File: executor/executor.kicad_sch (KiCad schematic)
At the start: 132 parts, among them J1 XT30PW(2+2), J2 gh1.25, 3p, J3 Conn_01x04, Q1 WNM6006, Q2 WNM6006, Q3 WNM6006, Q4 WNM6006, Q5 WNM6006, Q6 WNM6006, U1 WD1601E, U2 DRV8323SRTAT, U3 GD32F303RETx, U4 TCAN4550RGYRQ1, U5 AS5047P-ATSM, U6 QMA7981, Y1 8M, Y2 40M

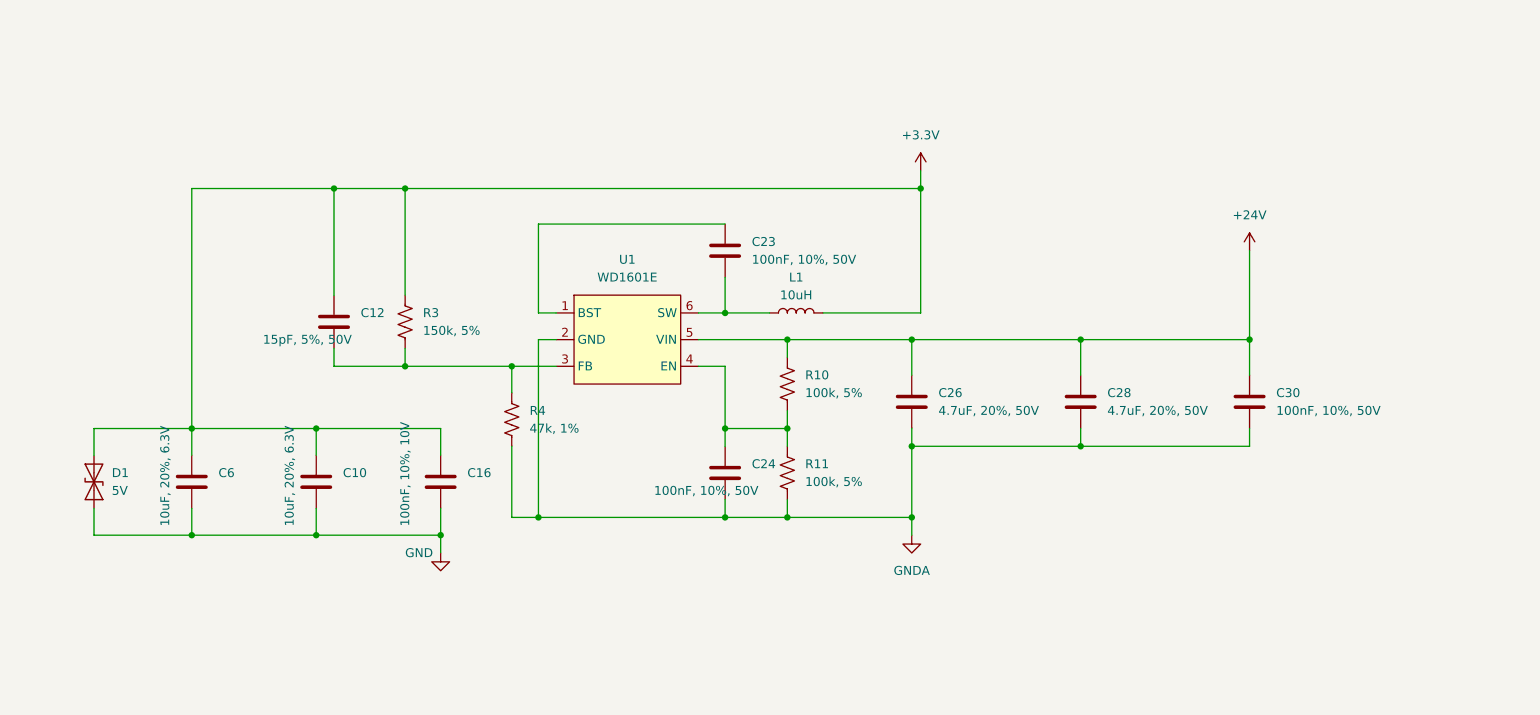
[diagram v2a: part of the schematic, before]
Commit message: [Fix] Replace dc-dc module to tps & fix xt30-2+2 position
Signed-off-by: Homalozoa <nx.tardis@gmail.com>
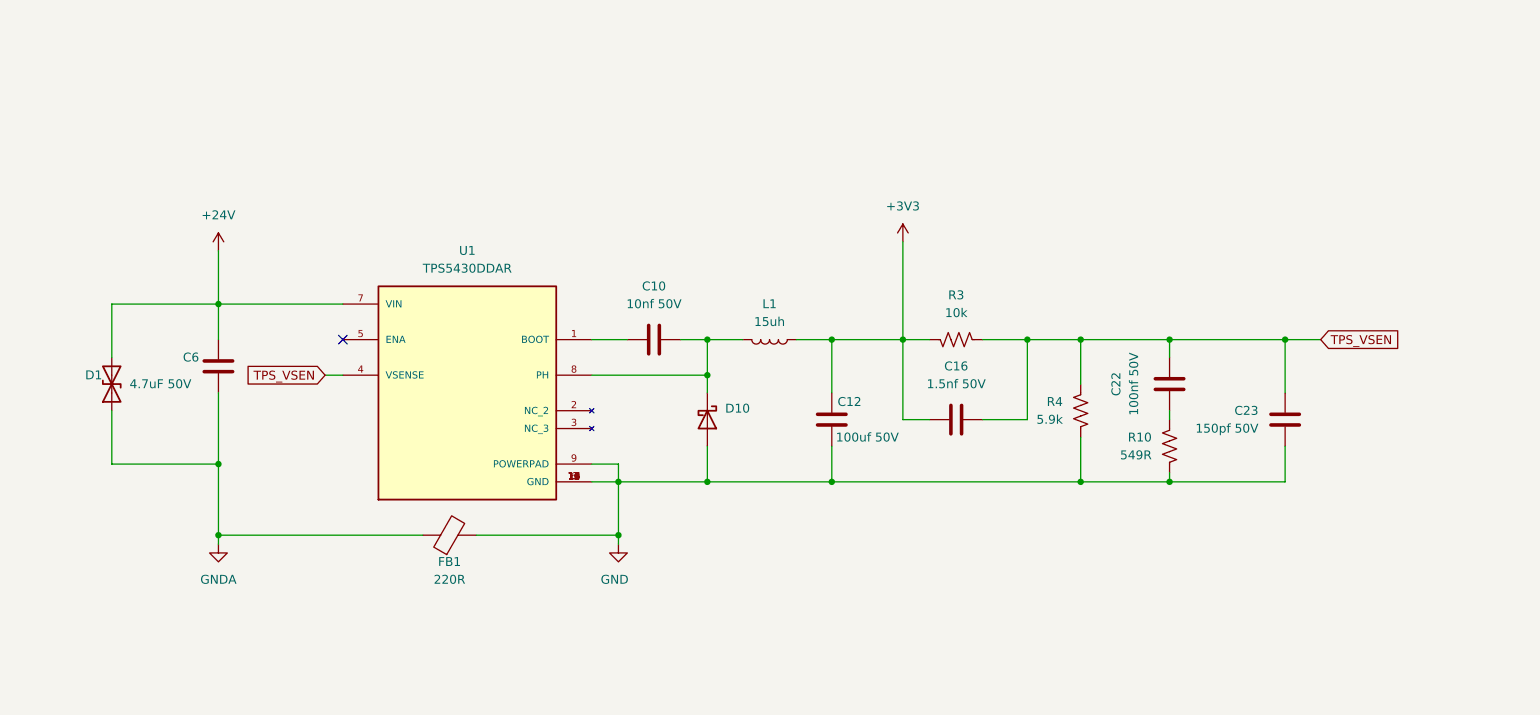
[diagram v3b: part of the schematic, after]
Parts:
- removed C24, C30: 100nF, 10%, 50V, Capacitor_SMD:C_0402_1005Metric, symbol Device:C
- removed C26, C28: 4.7uF, 20%, 50V, Capacitor_SMD:C_0805_2012Metric, symbol Device:C
- removed D1: 5V, Diode_SMD:D_SOD-923, symbol Diode:ESD9B5.0ST5G
- removed R11: 100k, 5%, Resistor_SMD:R_0402_1005Metric, symbol Device:R_US
- removed U1: WD1601E, Package_TO_SOT_SMD:SOT-23-6, symbol Rolling_Custom:WD1601E
- added C22: 100nf 50V, Capacitor_SMD:C_0402_1005Metric, symbol Device:C
- added D1: (no value), symbol Device:D_TVS
- added D10: (no value), symbol Diode:B340
- added FB1: 220R, Resistor_SMD:R_0603_1608Metric, symbol Device:FerriteBead
- added U1: TPS5430DDAR, Rolling_Custom:TPS5430DDAR, symbol Rolling_Custom:TPS5430DDAR
- C10: value 10uF, 20%, 6.3V -> 10nf 50V
- C12: value 15pF, 5%, 50V -> 100uf 50V; footprint Capacitor_SMD:C_0402_1005Metric -> Capacitor_SMD:C_0805_2012Metric
- C16: value 100nF, 10%, 10V -> 1.5nf 50V
- C23: value 100nF, 10%, 50V -> 150pf 50V
- C6: value 10uF, 20%, 6.3V -> 4.7uF 50V; footprint Capacitor_SMD:C_0402_1005Metric -> Capacitor_SMD:C_0805_2012Metric
- L1: value 10uH -> 15uh
- R10: value 100k, 5% -> 549R; footprint Resistor_SMD:R_0402_1005Metric -> Resistor_SMD:R_0201_0603Metric
- R3: value 150k, 5% -> 10k
- R4: value 47k, 1% -> 5.9k
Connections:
- net +24V: now also C6.1, D1.2 (A2), U1.7 (VIN); no longer R10.1
- net +3V3: now also C12.2, C16.2, L1.1, R3.2; no longer C10.1, C12.1, C16.1, C6.1, L1.2, R3.1
- net GND: now also C12.1, C23.2, R10.2, R4.2, D10.2 (A), FB1.2, U1.10 (GND), U1.11 (GND), U1.12 (GND), U1.13 (GND), U1.14 (GND), U1.15 (GND), U1.16 (GND), U1.17 (GND), U1.6 (GND), U1.9 (POWERPAD); no longer C10.2, C16.2, C6.2
- net GNDA: now also C6.2, D1.1 (A1), FB1.1; no longer R4.2
- net TPS_VSEN: now reaches C23.1
- net TPS_VSEN: now also C16.1, R3.1, R4.1, C22.1, U1.4 (VSENSE)
- new net: C22.2, R10.1
- new net: C10.2, D10.1 (K), L1.2, U1.8 (PH)
- new net: C10.1, U1.1 (BOOT)
- no-connect marks 30 -> 31

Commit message: [New] Replace TI's solution with TMC's in executor prj
1. DRV8323 --> TMC6200
2. GD32F303 --> TMC4671 + GD32C103
3. TCAN4550 --> GD32C103
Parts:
- removed C16: 1.5nf 50V, Capacitor_SMD:C_0402_1005Metric, symbol Device:C
- removed C22: 100nf 50V, Capacitor_SMD:C_0402_1005Metric, symbol Device:C
- removed C23: 150pf 50V, Capacitor_SMD:C_0402_1005Metric, symbol Device:C
- removed C25, C37: 1uF, 10%, 50V, Capacitor_SMD:C_0603_1608Metric, symbol Device:C
- removed C31, C34: 4.7uF, 20%, 50V, Capacitor_SMD:C_0805_2012Metric, symbol Device:C
- removed C32, C35: 1nF, 10%, 50V, Capacitor_SMD:C_0402_1005Metric, symbol Device:C
- removed C36: 100nF, 10%, 50V, Capacitor_SMD:C_0402_1005Metric, symbol Device:C
- removed C38: 20pF, 10%, 10V, Capacitor_SMD:C_0402_1005Metric, symbol Device:C
- removed C39: 100nF, 10%, 10V, Capacitor_SMD:C_0402_1005Metric, symbol Device:C
- removed C40: 10uF, 10%, 10V, Capacitor_SMD:C_0402_1005Metric, symbol Device:C
- removed C59: 470nF, 10%, 50V, Capacitor_SMD:C_0603_1608Metric, symbol Device:C
- removed D10: (no value), symbol Diode:B340
- removed D2, D4, D5, D6: BAV99, Package_TO_SOT_SMD:SOT-23, symbol Diode:BAV99
- removed D3: 30V, Diode_SMD:D_SMA, symbol Device:D_TVS
- removed D7: Blue, LED_SMD:LED_0402_1005Metric, symbol Device:LED
- removed D8, D9: 12V, Diode_SMD:D_SOD-323, symbol Device:D_TVS
- removed FB1: 220R, Resistor_SMD:R_0603_1608Metric, symbol Device:FerriteBead
- removed J1: XT30PW(2+2), Rolling_Custom:XT30PW(2+2), symbol Rolling_Custom:XT30PW(2+2)
- removed J2: gh1.25, 3p, Connector_JST:JST_GH_SM03B-GHS-TB_1x03-1MP_P1.25mm_Horizontal, symbol Connector:Conn_01x03_Female
- removed L1: 15uh, Inductor_SMD:L_0603_1608Metric, symbol Device:L
- removed NT1: NetTie, NetTie:NetTie-2_SMD_Pad0.5mm, symbol Device:NetTie_2
- removed Q1, Q2, Q3, Q4, Q5, Q6: WNM6006, Rolling_Custom:PDFN5X6-8L, symbol Rolling_Custom:WNM6006
- removed R27: 10k, 5%, Resistor_SMD:R_0402_1005Metric, symbol Device:R_US
- removed R30: 0R, 5%, Resistor_SMD:R_0402_1005Metric, symbol Device:R_US
- removed R4: 5.9k, Resistor_SMD:R_0402_1005Metric, symbol Device:R_US
- removed TP10: C, TestPoint:TestPoint_Plated_Hole_D2.0mm, symbol Connector:TestPoint
- removed TP7: A, TestPoint:TestPoint_Plated_Hole_D2.0mm, symbol Connector:TestPoint
- removed TP8: B, TestPoint:TestPoint_Plated_Hole_D2.0mm, symbol Connector:TestPoint
- removed U1: TPS5430DDAR, Rolling_Custom:TPS5430DDAR, symbol Rolling_Custom:TPS5430DDAR
- removed U2: DRV8323SRTAT, Rolling_Custom:WQFN40, symbol Rolling_Custom:DRV8323SRTAT
- removed U3: GD32F303RETx, Package_QFP:LQFP-64_10x10mm_P0.5mm, symbol Rolling_Custom:GD32F303RETx
- removed U4: TCAN4550RGYRQ1, Rolling_Custom:VQFN20, symbol Rolling_Custom:TCAN4550RGYRQ1
- removed Y2: 40M, Oscillator:Oscillator_SMD_ECS_2520MV-xxx-xx-4Pin_2.5x2.0mm, symbol Device:Crystal_GND24
- added C1, C11, C13, C3, C4, C63, C7, C8: 100nF/50V/0402, Capacitor_SMD:C_0402_1005Metric, symbol Device:C
- added C14: 22nF/50V/0603, Capacitor_SMD:C_0603_1608Metric, symbol Device:C
- added C19, C26: 100nF/100V/0805, Capacitor_SMD:C_0805_2012Metric, symbol Device:C
- added C2: 4.7uF/50V/0402, Capacitor_SMD:C_0402_1005Metric, symbol Device:C
- added C28, C30: 470nF/50V/0603, Capacitor_SMD:C_0603_1608Metric, symbol Device:C
- added C56: 4.7uF/10V/0402, Capacitor_SMD:C_0402_1005Metric, symbol Device:C
- added C57: 20pF/10V/0402, Capacitor_SMD:C_0402_1005Metric, symbol Device:C
- added C58: 1uF/10V/0402, Capacitor_SMD:C_0402_1005Metric, symbol Device:C
- added C61: 8.2nf/50V/0603, Capacitor_SMD:C_0603_1608Metric, symbol Device:C
- added C67: 22uF/6.3V/0402, Capacitor_SMD:C_0402_1005Metric, symbol Device:C
- added C68, C69: 47uf/50V/0603, Capacitor_SMD:C_0603_1608Metric, symbol Device:C
- added C71, C72: 100pF/50V/0402, Capacitor_SMD:C_0402_1005Metric, symbol Device:C
- added C73: 2.2uF/50V/0603, Capacitor_SMD:C_0603_1608Metric, symbol Device:C
- added C9: 2.2uF/100V/1210, Capacitor_SMD:C_1210_3225Metric, symbol Device:C
- added D2: BZT52C24, Diode_SMD:D_SOD-123F, symbol Diode:BZT52Bxx
- added D3: BZT52C5V1S, Diode_SMD:D_SOD-123F, symbol Diode:BZT52Bxx
- added D4, D5: 12V, Diode_SMD:D_SOD-323, symbol Device:D_TVS
- added J1: PowerOutput, Connector_AMASS:AMASS_XT30UPB-M_1x02_P5.0mm_Vertical, symbol Connector:Conn_01x02_Female
- added J2: SWD_DBG_Mounting, Connector_JST:JST_GH_SM03B-GHS-TB_1x03-1MP_P1.25mm_Horizontal, symbol Connector_Generic_MountingPin:Conn_01x03_MountingPin
- added J4: CAN_FD, Connector_JST:JST_GH_SM04B-GHS-TB_1x04-1MP_P1.25mm_Horizontal, symbol Connector_Generic_MountingPin:Conn_01x04_MountingPin
- added J5: RTMI, Rolling_Custom:FH34SRJ-6S-0.5SH50, symbol Connector_Generic:Conn_01x08
- added L3: 15uh, SLO0530H150MTT, Inductor_SMD:L_Sunlord_MWSA0518_5.4x5.2mm, symbol Device:L
- added L4: LQW15AN1N3D10D, Inductor_SMD:L_0402_1005Metric, symbol Device:L
- added Q1, Q2, Q3, Q4, Q5, Q6: BSC0702LS, Package_TO_SOT_SMD:TDSON-8-1, symbol Transistor_FET:BSC070N10NS5
- added R11: 22R/1%/0603, Resistor_SMD:R_0603_1608Metric, symbol Device:R_US
- added R17: 1k/1%/0603, Resistor_SMD:R_0603_1608Metric, symbol Device:R_US
- added R2: 0.003R/1%/1W/1206, Resistor_SMD:R_1206_3216Metric, symbol Device:R_US
- added R24: 20.5k/0402, Resistor_SMD:R_0402_1005Metric, symbol Device:R_US
- added R25: 10k/5%/0402, Resistor_SMD:R_0402_1005Metric, symbol Device:R_US
- added R35, R36: 0R/0402, Resistor_SMD:R_0402_1005Metric, symbol Device:R_US
- added TP1: U, TestPoint:TestPoint_Plated_Hole_D2.0mm, symbol Connector:TestPoint
- added TP2: V, TestPoint:TestPoint_Plated_Hole_D2.0mm, symbol Connector:TestPoint
- added TP3: W, TestPoint:TestPoint_Plated_Hole_D2.0mm, symbol Connector:TestPoint
- added U1: TMC4671-LA, Rolling_Custom:QFN76_10P5X6P5_TRI, symbol Rolling_Custom:TMC4671-LA
- added U2: TJA1042T, Package_SO:SOIC-8_3.9x4.9mm_P1.27mm, symbol Interface_CAN_LIN:TJA1042T
- added U3: TMC6200-TA, Rolling_Custom:eTQFP48_9x9_TRI, symbol Rolling_Custom:TMC6200-TA
- added U6: TPS54231, Package_SO:SOIC-8_3.9x4.9mm_P1.27mm, symbol Regulator_Switching:TPS54233
- added U7: AMS1117-3.3, Package_TO_SOT_SMD:SOT-223-3_TabPin2, symbol Regulator_Linear:AMS1117-3.3
- added U8: GD32C103TBUx, Rolling_Custom:QFN-36-1EP_6x6mm_P0.5mm, symbol Rolling_Custom:GD32C103TBUx
- added X1: XO32, Oscillator:Oscillator_SMD_EuroQuartz_XO32-4Pin_3.2x2.5mm, symbol Oscillator:XO32
- C10: value 10nf 50V -> 2.2uF/100V/1210; footprint Capacitor_SMD:C_0402_1005Metric -> Capacitor_SMD:C_1210_3225Metric
- C12: value 100uf 50V -> 2.2uF/50V/0603; footprint Capacitor_SMD:C_0805_2012Metric -> Capacitor_SMD:C_0603_1608Metric
- C15: renamed from C1; value 10uF, 20%, 50V -> 10uF/50V/0805
- C16: renamed from C2; value 10uF, 20%, 50V -> 10uF/50V/0805
- C17: renamed from C61; value 100nF, 10%, 10V -> 100nF/10V/0402
- C18: renamed from C3; value 10uF, 20%, 50V -> 10uF/50V/0805
- C20: renamed from C4; value 10uF, 20%, 50V -> 10uF/50V/0805
- C21: renamed from C63; value 1uF, 10%, 10V -> 1uF/10V/0402
- C22: renamed from C5; value 10uF, 20%, 50V -> 10uF/50V/0805
- C23: renamed from C7; value 10uF, 20%, 50V -> 10uF/50V/0805
- C24: renamed from C8; value 10uF, 20%, 50V -> 10uF/50V/0805
- C25: renamed from C9; value 10uF, 20%, 50V -> 10uF/50V/0805
- C27: renamed from C11; value 10uF, 20%, 50V -> 10uF/50V/0805
- C29: value 1uF, 10%, 50V -> 470nF/50V/0603
- C31: renamed from C13; value 10uF, 20%, 50V -> 10uF/50V/0805
- C32: renamed from C56; value 10nF, 10%, 10V -> 10nF/10V/0402
- C33: renamed from C14; value 10uF, 20%, 50V -> 10uF/50V/0805
- C34: renamed from C15; value 10uF, 20%, 50V -> 10uF/50V/0805
- C35: renamed from C57; value 2.2uF, 10%, 10V -> 2.2uF/10V0402
- C36: renamed from C18; value 10uF, 20%, 50V -> 10uF/50V/0805
- C37: renamed from C19; value 10uF, 20%, 50V -> 10uF/50V/0805
- C38: renamed from C58; value 100nnF, 10%, 10V -> 100nF/10V/0402
- C39: renamed from C20; value 10uF, 20%, 50V -> 10uF/50V/0805
- C40: renamed from C21; value 10uF, 20%, 50V -> 10uF/50V/0805
- C41: value 100nF, 10%, 10V -> 10pf/50V/0402
- C42: value 20pF, 10%, 10V -> 10uF/10V/0402
- C43: value 100nF, 10%, 10V -> 100nF/50V/0402
- C44, C46, C52: value 100nF, 10%, 10V -> 100nF/10V/0402
- C45: value 10uF, 10%, 10V -> 1.5nf/50V/0603; footprint Capacitor_SMD:C_0402_1005Metric -> Capacitor_SMD:C_0603_1608Metric
- C47: value 4.7uF, 10%, 10V -> 10uF/10V/0402
- C48: value 1uF, 10%, 10V -> 100nF/10V/0402
- C49: value 47nF, 10%, 50V -> 100nF/10V/0402
- C5: renamed from C17; value 1uF, 10%, 50V -> 2.2uF/100V/1210; footprint Capacitor_SMD:C_0603_1608Metric -> Capacitor_SMD:C_1210_3225Metric
- C50: value 1uF, 10%, 10V -> 20pF/10V/0402
- C51: value 100nF, 10%, 10V -> 4.7uF/50V/0805; footprint Capacitor_SMD:C_0402_1005Metric -> Capacitor_SMD:C_0805_2012Metric
- C53: value 10pF, 10%, 50V -> 100nF/50V/0402
- C54: value 10nF, 10%, 50V -> 4.7uF/50V/0805; footprint Capacitor_SMD:C_0402_1005Metric -> Capacitor_SMD:C_0805_2012Metric
- C55: value 10pF, 10%, 50V -> 10uf/50V/0402
- C59: renamed from C27; value 100nF, 10%, 10V -> 100nF/10V/0402
- C6: value 4.7uF 50V -> 100nF/50V/0402; footprint Capacitor_SMD:C_0805_2012Metric -> Capacitor_SMD:C_0402_1005Metric
- C60: value 100pF, 10%, 10V -> 100nF/10V/0402
- C62: value 100pF, 10%, 10V -> 10uf/50V/0402
- C64: value 100nF, 10%, 50V -> 100nF/10V/0402
- C65: value 10uF, 10%, 50V -> 10uf/50V/0402; footprint Capacitor_SMD:C_0603_1608Metric -> Capacitor_SMD:C_0402_1005Metric
- C66: value 10uF, 10%, 50V -> 100nF/50V/0402; footprint Capacitor_SMD:C_0603_1608Metric -> Capacitor_SMD:C_0402_1005Metric
- C70: renamed from C33; value 100nF, 10%, 10V -> 100nF/10V/0402
- D1: value (none) -> SMF30CA; footprint (none) -> Diode_SMD:D_SOD-123
- J3: value Conn_01x04 -> SWD_DBG
- L2: value 20R -> FCM1608KF-100T07; footprint Resistor_SMD:R_0402_1005Metric -> Resistor_SMD:R_0603_1608Metric
- R1, R12, R13, R7: value 0 -> 22R/1%/0603; footprint Resistor_SMD:R_0402_1005Metric -> Resistor_SMD:R_0603_1608Metric
- R10: value 549R -> 22R/1%/0603; footprint Resistor_SMD:R_0201_0603Metric -> Resistor_SMD:R_0603_1608Metric
- R14: renamed from R36; value 2.2k, 5% -> 4.7k/5%/0402
- R15: renamed from R37; value 2.2k, 5% -> 4.7k/5%/0402
- R16: value 0.001R -> 4k7/1%/0603; footprint Resistor_SMD:R_1206_3216Metric -> Resistor_SMD:R_0603_1608Metric
- R18: value 10k, 5% -> 64.9k/0402
- R19: value 0 -> 0r/0402
- R20: value 10k, 5% -> 10k/5%/0402
- R21, R22: value 100R, 5% -> 4k7/1%/0603; footprint Resistor_SMD:R_0402_1005Metric -> Resistor_SMD:R_0603_1608Metric
- R23: value 100R, 5% -> 169k/0402
- R26: renamed from R14; value 10k, 5% -> 10k/5%/0402
- R27: renamed from R15; value 10k, 5% -> 10k/5%/3477K/0402
- R28: value 0R, 5% -> 10.2k/0402
- R29: value 0R, 5% -> 1.96k/0402
- R3: value 10k -> 0.003R/1%/1W/1206; footprint Resistor_SMD:R_0402_1005Metric -> Resistor_SMD:R_1206_3216Metric
- R30: renamed from R17; value 10k, 5% -> 10k/5%/0402
- R31: value 100R, 5% -> 120R/0402
- R32: value 33k -> 4.7k/5%/0402
- R33: value 330R, 5% -> 0R/0402
- R34: value 3k -> 0R/0402
- R4: renamed from R2; value 0 -> 22R/1%/0603; footprint Resistor_SMD:R_0402_1005Metric -> Resistor_SMD:R_0603_1608Metric
- R5: value 150k, 5% -> 22R/1%/0603; footprint Resistor_SMD:R_0402_1005Metric -> Resistor_SMD:R_0603_1608Metric
- R6: value 10k, 5% -> 10k/1%/0402
- R8: value 0 -> 0.003R/1%/1W/1206; footprint Resistor_SMD:R_0402_1005Metric -> Resistor_SMD:R_1206_3216Metric
- R9: value 0.001R -> 0.003R/1%/1W/1206
- renumbered TP13 to TP4, TP14 to TP5, U6 to U4
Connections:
- net CAN_H is gone; now on net GND: C62.2
- net CAN_L is gone; now on net GND: C60.2
- net ECD_MISO is gone; now on an unnamed net: U5.3 (MISO)
- net IBP is gone; now on net V: R9.1
- net ISENSE_A is gone; now on net +5V: R21.1
- net ISENSE_B is gone; now on net +2.5V_REF: R22.1
- net ISENSE_C is gone; now on net +24V: R23.1
- net PWM_A is gone; now on net 5V_FB: R28.2
- net PWM_B is gone; now on net GND: R29.2
- net TCAN_OSC_IN is gone; now on net +2.5V_REF: C53.2
- net TCAN_OSC_OUT is gone; now on net GND: C55.2
- net TPS_VSEN is gone; now on net U: R3.1
- net VGL_B is gone; now on net V: R8.1
- net +24V: now also C10.2, C51.1, C54.1, C55.1, R16.1, C11.2, C19.1, C26.1, C9.2, D2.1 (K), J1.2 (Pin_2), Q1.5 (D), Q3.5 (D), Q5.5 (D), U3.29 (VSA), U3.33 (VS), U6.2 (VIN); no longer C29.2, C6.1, C64.1, C65.1, R34.1, R5.1
- net +3V3: now also C42.2, C44.2, C49.1, C60.1, R20.1, R32.2, R6.1, C1.2, C13.2, C56.1, C58.1, L4.2, R36.2, U1.13 (VCCIO2), U1.2 (VCCIO1), U1.43 (VCCIO3), U1.52 (VCCIO4), U1.61 (VCCIO5), U1.72 (VCCIO6), U3.19 (VCC_IO), U8.1 (VDD), U8.19 (VDD), U8.27 (VDD), X1.4 (V+); no longer C12.2, C41.1, C43.2, C44.1, C47.1, C50.1, C51.1, R18.1, R20.2, R3.2, U4.10 (SENB/SCS)
- net ACC_INT1: now also U8.32 (PB5)
- net ACC_INT2: now also U8.31 (PB4)
- net ACC_SCL: now also U8.33 (PB6)
- net ACC_SDA: now also U8.34 (PB7)
- net DRV_EN: now also U1.32 (ENO), U3.27 (DRV_EN)
- net DRV_SCS: now also U3.13 (CSN_IDRV0), U8.20 (PA8)
- net ECD_SCS: now also R34.2, U8.21 (PA9); no longer U5.1 (CSN)
- net GND: now also C10.1, C15.2, C16.2, C18.2, C20.2, C22.2, C23.2, C24.2, C25.2, C27.2, C31.2, C33.2, C34.2, C36.2, C37.2, C39.2, C40.2, C44.1, C45.2, C46.2, C49.2, C5.1, C50.1, C54.2, C6.1, D1.1 (A1), R22.2, C1.1, C11.1, C13.1, C2.2, C26.2, C3.1, C4.1, C56.2, C57.1, C58.2, C61.2, C63.2, C67.2, C68.2, C69.2, C7.1, C71.1, C72.1, C73.1, C8.1, C9.1, D2.2 (A), D3.2 (A), D4.2 (A2), D5.2 (A2), J1.1 (Pin_1), J2.3 (Pin_3), J2.MP (MountPin), J4.MP (MountPin), J5.6 (Pin_6), J5.7 (Pin_7), J5.8 (Pin_8), Q2.1 (S), Q2.2 (S), Q2.3 (S), Q4.1 (S), Q4.2 (S), Q4.3 (S), Q6.1 (S), Q6.2 (S), Q6.3 (S), R17.2, R24.2, R25.2, U1.14 (GNDIO2), U1.24 (GNDA), U1.3 (GNDIO1), U1.44 (GNDIO3), U1.53 (GNDIO4), U1.54 (TEST), U1.59 (PWM_IDLE_H), U1.60 (PWM_IDLE_L), U1.62 (GNDIO5), U1.73 (GNDIO6), U1.77 (EPAD), U2.2 (GND), U3.24 (CLK), U3.8 (GNDA), U3.EPAD, U6.7 (GND), U7.1 (GND), U8.18 (VSS), U8.26 (VSS), U8.36 (VSS), X1.2 (GND); no longer C44.2, C47.2, C48.2, C50.2, C54.1, C55.1, C60.1, C62.1, C64.2, R10.2, R33.2, R6.2
- net MCU_OSC_IN: now also C50.2, U8.2 (PD0-OSCIN)
- net MCU_OSC_OUT: now also C57.2, U8.3 (PD1-OSCOUT); no longer C42.2
- net NRST: now also C46.1, R20.2, U8.4 (NRST); no longer R18.2
- net SWCLK: now also J2.2 (Pin_2), U8.28 (PA14)
- net SWDIO: now also J2.1 (Pin_1), U8.25 (PA13)
- net TEMP_BOARD: now also U8.8 (PA1)
- net TEMP_MOTOR: now also U8.7 (PA0)
- net HSV: now reaches R10.1
- net HSV: now also U3.43 (HSV)
- net CANFD_H: now reaches R31.1
- net CANFD_H: now also C72.2, D5.1 (A1), J4.1 (Pin_1), J4.2 (Pin_2), U2.7 (CANH)
- net U: now reaches R1.2
- net U: now also R2.1, TP1.1
- net at R23.2: now also R24.1, U6.3 (EN)
- net +2.5V_REF: now reaches R21.2
- net +2.5V_REF: now also U1.17 (ADC_I0_NEG), U1.19 (ADC_I1_NEG), U3.12 (VOFS/TEST)
- net VREF-: now reaches C48.1
- net VREF-: now also C47.1, R19.2, U8.5 (VSSA)
- net 5V_FB: now reaches R29.1
- net 5V_FB: now also U6.5 (FB)
- net BMV: now reaches R8.2
- net BMV: now also C29.2, R9.2, Q3.1 (S), Q3.2 (S), Q3.3 (S), Q4.5 (D), U3.42 (V)
- net at R13.2: now also Q6.4 (G)
- net V: now reaches R7.2
- net V: now also TP2.1
- net +5V: now reaches R28.1
- net +5V: now also C62.1, C2.1, C3.2, C63.1, C68.1, C69.1, D3.1 (K), L3.1, U1.23 (V5), U2.3 (VCC), U7.3 (VI)
- net at R12.2: now also Q5.4 (G)
- net at R4.2: now also Q1.4 (G)
- net ECD_MOSI: no longer names the net of U5.4 (MOSI)
- net ECD_MOSI: now also R35.1
- net ECD_SCK renamed EXE_SCK
- net EXE_SCK: now also U1.7 (SPI_SCK), U3.14 (SCK_IDRV1), U8.12 (PA5)
- removed net GNDA: C15.2, C16.2, C18.2, C20.2, C22.2, C23.2, C24.2, C25.2, C27.2, C31.2, C33.2, C34.2, C36.2, C37.2, C39.2, C40.2, C5.1, C6.2, D1.1 (A1), R16.2, R9.2
- net ICP: no longer names the net of C29.1
- net ICP: now also U3.44 (CV); no longer R16.1
- net TCAN_WAKE: no longer names the net of R32.1
- net TCAN_WAKE: now also U4.10 (SENB/SCS)
- net VCCOUT: no longer names the net of C66.1
- net VCCOUT: now also C65.1, C67.1, L4.1, U7.2 (VO)
- net VGH_A renamed HSU
- net HSU: now also U3.48 (HSU)
- net VGH_B renamed VSENSE
- net VSENSE: now also U3.41 (VSENSE)
- net VGH_C renamed HSW
- net HSW: now also U3.37 (HSW)
- net VGL_A renamed USENSE
- net USENSE: now also U3.46 (USENSE)
- net VGL_C renamed LSW
- net LSW: now also U3.3 (LSW)
- removed net VREF_D: C45.2, C46.2, L2.2
- removed net VREF_S: C45.1, C46.1, R19.2
- removed net VSEN_BUS: R31.2, R5.2, R6.1
- new net: R34.1, U5.1 (CSN)
- new net: Q3.4 (G), R10.2
- new net: C7.2, U1.45 (VCCCORE2)
- new net: C8.2, U1.63 (VCCCORE3)
- new net: C6.2, U1.15 (VCCCORE1)
- new net: C4.2, R6.2, U1.50 (NRST)
- new net: C28.1, U3.1 (CU)
- new net: R36.1, U3.25 (SPE)
- new net: C14.2, U3.30 (CPO)
- new net: C14.1, U3.32 (CPI)
- new net: C19.2, U3.34 (VCP)
- new net: C30.1, U3.36 (CW)
- new net: C73.2, U3.6 (12VOUT)
- new net: C12.2, U3.7 (5VOUT)
- new net: C45.1, R18.2
- new net: Q4.4 (G), R11.2
- new net: C64.2, U6.1 (BOOT)
- new net: C61.1, U6.4 (SS)
- new net: C64.1, L3.2, U6.8 (PH)
- new net: R25.1, U8.35 (BOOT0)
- new net: Q2.4 (G), R5.2
- new net 5V_CMP: C41.1, R18.1, U6.6 (COMP)
- new net ADC_VM: C43.2, R16.2, R17.1, U1.20 (ADC_VM)
- new net BMU: C28.2, Q1.1 (S), Q1.2 (S), Q1.3 (S), Q2.5 (D), R2.2, R3.2, U3.47 (U)
- new net CANFD_L: C71.2, D4.1 (A1), J4.3 (Pin_3), J4.4 (Pin_4), R31.2, U2.6 (CANL)
- new net CANFD_RX: U2.4 (RXD), U8.23 (PA11)
- new net CANFD_TX: U2.1 (TXD), U8.24 (PA12)
- new net CURU: U1.16 (ADC_I0_POS), U3.9 (CURU)
- new net CURV: U1.18 (ADC_I1_POS), U3.10 (CURV)
- new net DBG_SCK: J5.2 (Pin_2), U1.76 (GPIO4/AGPI_B_MCD/DBGSPI_SCK)
- new net DBG_SCS: J5.1 (Pin_1), U1.75 (GPIO3/AGPI_A_MCD/DBGSPI_NSCS)
- new net DBG_SDI: J5.3 (Pin_3), U1.1 (GPIO5/AENC_UX_MCD/DBGSPI_MOSI)
- new net DBG_SDO: J5.4 (Pin_4), U1.4 (GPIO6/AENC_VN_MCD/DBGSPI_MISO)
- new net DBG_TRG: J5.5 (Pin_5), U1.5 (GPIO7/AENC_WY_MCD/DBGSPI_TRG)
- new net DRV_FAULT: U3.26 (FAULT), U8.30 (PB3)
- new net EXE_SDI: R35.2, U1.8 (SPI_MOSI), U3.15 (SDI_AMPLX10), U8.14 (PA7)
- new net EXE_SDO: R33.2, U1.9 (SPI_MISO), U3.16 (SDO_SINGLE), U8.13 (PA6)
- new net FOC_CLK: U1.51 (CLK), X1.3 (OUT)
- new net FOC_EN: U1.55 (ENI), U8.16 (PB1)
- new net FOC_OSC_EN: U8.15 (PB0), X1.1 (EN)
- new net FOC_RXD: U1.10 (UART_RXD), U8.9 (PA2)
- new net FOC_SCS: U1.6 (SPI_NSCS), U8.11 (PA4)
- new net FOC_STATUS: U1.12 (STATUS), U8.17 (PB2)
- new net FOC_TXD: U1.11 (UART_TXD), U8.10 (PA3)
- new net LSU: R5.1, U3.5 (LSU)
- new net LSV: R11.1, U3.4 (LSV)
- new net UH: U1.39 (PWM_UX1_H), U3.17 (UH)
- new net UL: U1.40 (PWM_UX1_L), U3.18 (UL)
- new net VH: U1.41 (PWM_VX2_H), U3.20 (VH)
- new net VL: U1.42 (PWM_VX2_L), U3.21 (VL)
- new net VREF+: C47.2, C48.2, L2.2, U8.6 (VDDA)
- new net W: C30.2, Q5.1 (S), Q5.2 (S), Q5.3 (S), Q6.5 (D), TP3.1, U3.38 (W), U3.39 (WSENSE)
- new net WH: U1.46 (PWM_WY1_H), U3.22 (WH)
- new net WL: U1.47 (PWM_WY1_L), U3.23 (WL)
- no-connect marks 31 -> 42
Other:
- note added: "Absolute position encoder"
- note added: "CAN FD bus transceiver"
- note added: "DC 24V to DC 5V converter"
- note added: "DC 5V to DC 3V3 converter"
- note added: "FOC circuits"
- note added: "GDC103 MCU & its peripherals"
- note added: "High range accelerometer"
- note added: "Power flags & ports"
- company: (none) -> cyber-zoo
- title: Executor -> Rolling executor
- moved on the sheet: C15, C16, C17, C18, C20, C21, C22, C23, C24, C25, C27, C31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

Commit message: [New] Complete PCB layout of executor v2.0
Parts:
- removed R34, R35: 0R/0402, Resistor_SMD:R_0402_1005Metric, symbol Device:R_US
- added J6: DebugSPI, Rolling_Custom:FH34SRJ-6S-0.5SH50, symbol Connector_Generic:Conn_01x08
- C55: value 10uf/50V/0402 -> 10uf/50V/0805; footprint Capacitor_SMD:C_0402_1005Metric -> Capacitor_SMD:C_0805_2012Metric
- L3: value 15uh, SLO0530H150MTT -> 15uh/SLO0530H150MTT
- X1: value XO32 -> X1G004241012811; footprint Oscillator:Oscillator_SMD_EuroQuartz_XO32-4Pin_3.2x2.5mm -> Crystal:Crystal_SMD_3225-4Pin_3.2x2.5mm
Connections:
- net DRV_SCS: now also J6.1 (Pin_1)
- net ECD_SCS: now also R33.1, U5.1 (CSN); no longer U8.21 (PA9)
- net EXE_SCK: now also J6.2 (Pin_2)
- net EXE_SDI: now also U5.4 (MOSI), J6.3 (Pin_3)
- net EXE_SDO: now also U5.3 (MISO), J6.4 (Pin_4); no longer R33.2
- net FOC_SCS: now also J6.5 (Pin_5)
- net GND: now also J6.6 (Pin_6), J6.7 (Pin_7), J6.8 (Pin_8)
- new net: R33.2, U8.21 (PA9)
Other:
- moved on the sheet: D1, D2, J1, J2, J3, J4, J5, TP1, TP2, TP3

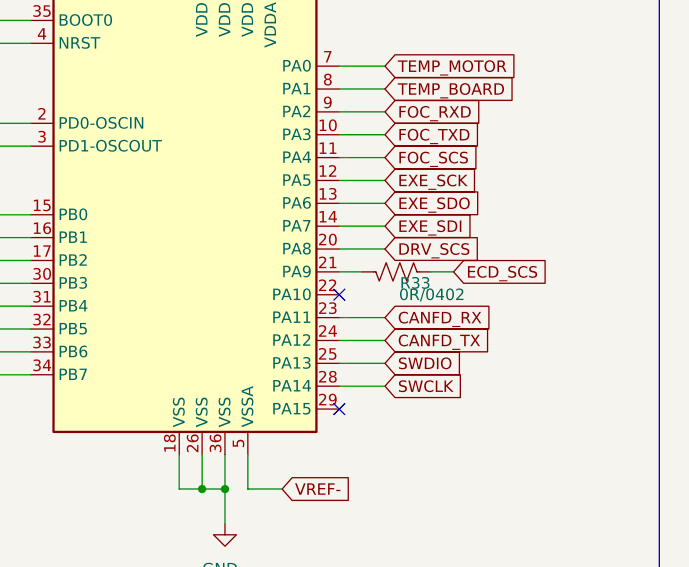
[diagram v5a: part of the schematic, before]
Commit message: [Fix] Move components to avoid collisions
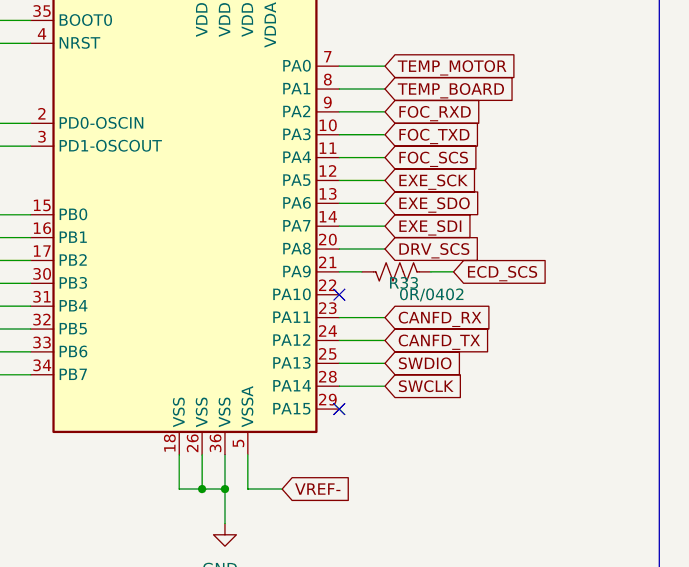
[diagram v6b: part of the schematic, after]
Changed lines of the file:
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@@
     (stroke (width 0) (type default) (color 0 0 0 0))
   )
+  (wire (pts (xy 535.94 233.68) (xy 538.48 233.68))
+    (stroke (width 0) (type default) (color 0 0 0 0))
+  )
   (wire (pts (xy 439.42 104.14) (xy 439.42 106.68))
     (stroke (width 0) (type default) (color 0 0 0 0))
@@
     (stroke (width 0) (type default) (color 0 0 0 0))
   )
-  (wire (pts (xy 535.94 233.68) (xy 538.48 233.68))
-    (stroke (width 0) (type default) (color 0 0 0 0))
-  )
   (wire (pts (xy 539.75 158.75) (xy 539.75 162.56))
     (stroke (width 0) (type default) (color 0 0 0 0))
@@
   (symbol (lib_id "Device:R_US") (at 542.29 233.68 270) (mirror x) (unit 1)
     (in_bom yes) (on_board yes)
-    (property "Reference" "R33" (id 0) (at 546.1 234.95 90)
+    (property "Reference" "R33" (id 0) (at 544.83 234.95 90)
       (effects (font (size 1.27 1.27)) (justify right))
     )

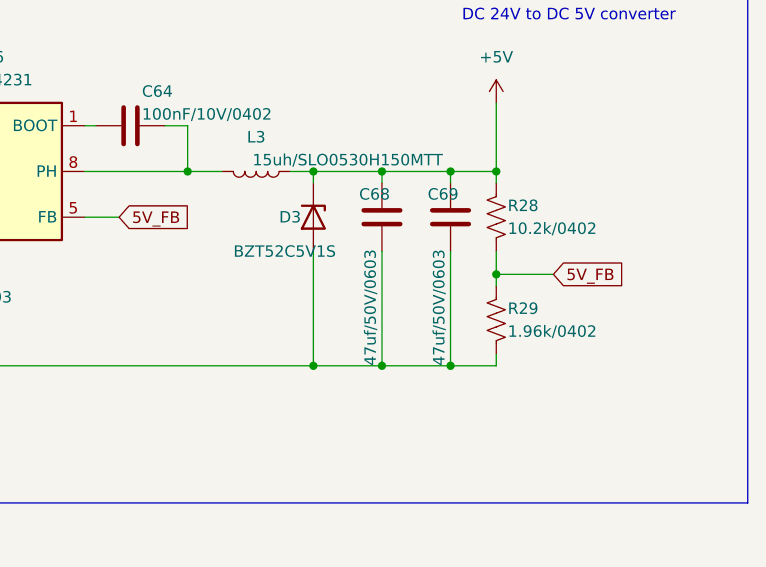
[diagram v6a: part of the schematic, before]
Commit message: [Fix] Correct capacities in 24Vto5V converter
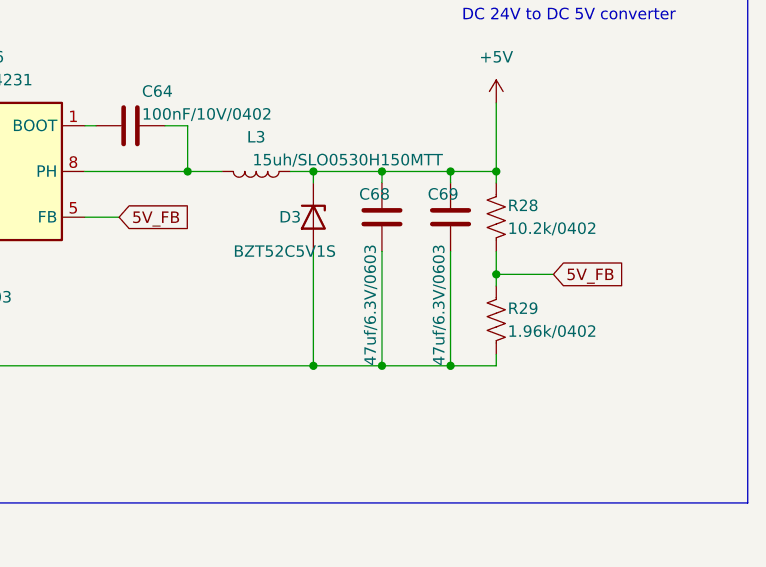
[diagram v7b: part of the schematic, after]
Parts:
- C68, C69: value 47uf/50V/0603 -> 47uf/6.3V/0603
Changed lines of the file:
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@@
       (effects (font (size 1.27 1.27)) (justify left))
     )
-    (property "Value" "47uf/50V/0603" (id 1) (at 530.86 64.77 90)
+    (property "Value" "47uf/6.3V/0603" (id 1) (at 530.86 64.77 90)
       (effects (font (size 1.27 1.27)) (justify left))
     )
@@
       (effects (font (size 1.27 1.27)) (justify left))
     )
-    (property "Value" "47uf/50V/0603" (id 1) (at 538.48 64.77 90)
+    (property "Value" "47uf/6.3V/0603" (id 1) (at 538.48 64.77 90)
       (effects (font (size 1.27 1.27)) (justify left))
     )
@@
     )
     (path "/37357377-e9e2-4a2d-9221-58525e53f1fa"
-      (reference "C68") (unit 1) (value "47uf/50V/0603") (footprint "Capacitor_SMD:C_0603_1608Metric")
+      (reference "C68") (unit 1) (value "47uf/6.3V/0603") (footprint "Capacitor_SMD:C_0603_1608Metric")
     )
     (path "/f338e9a5-4087-4d58-b431-c94fb7478c23"
-      (reference "C69") (unit 1) (value "47uf/50V/0603") (footprint "Capacitor_SMD:C_0603_1608Metric")
+      (reference "C69") (unit 1) (value "47uf/6.3V/0603") (footprint "Capacitor_SMD:C_0603_1608Metric")
     )
     (path "/8e0128b9-ddfc-44b2-8b62-80ee9fa07549"
